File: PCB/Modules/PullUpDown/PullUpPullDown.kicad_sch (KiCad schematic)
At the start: 7 parts

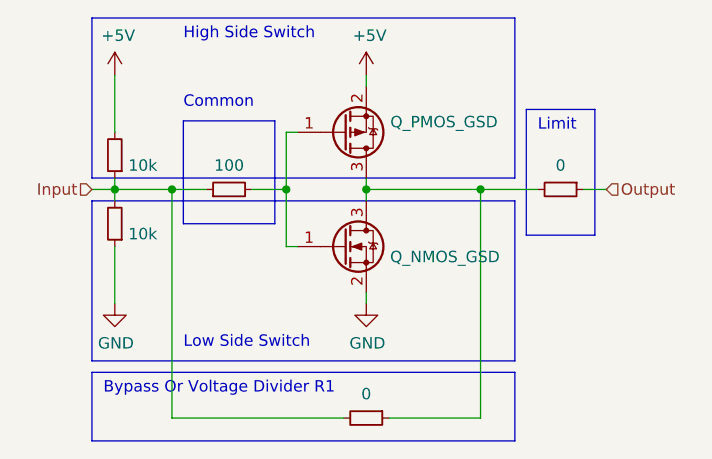
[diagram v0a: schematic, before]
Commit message: Upgrade KiCad files from 6.0 to 7.0.
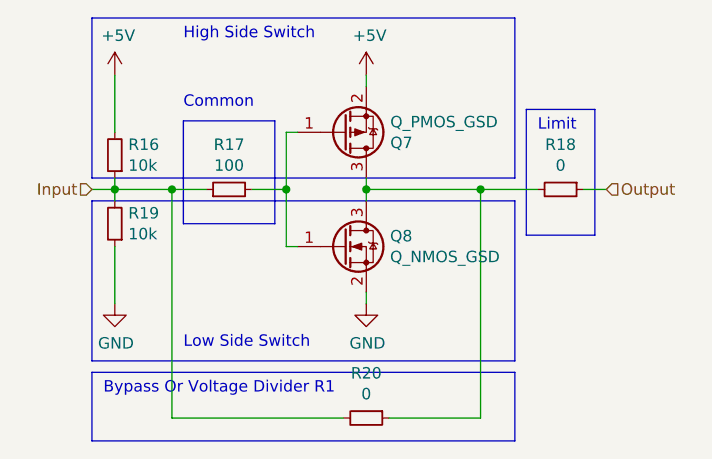
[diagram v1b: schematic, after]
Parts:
- gave numbers to parts that had none: 7

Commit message: First pass of PCB rework.
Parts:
- removed R20: 0, Resistor_SMD:R_0805_2012Metric, symbol Device:R_Small
- added JP1: Bypass, Jumper:SolderJumper-2_P1.3mm_Open_RoundedPad1.0x1.5mm, symbol Jumper:SolderJumper_2_Open
- renumbered Q7 to Q1, Q8 to Q2, R16 to R1, R19 to R2, R17 to R3, R18 to R4
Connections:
- net Input: now also JP1.1 (A)
- net at Q1.3 (D), Q2.3 (D), R4.2: now also JP1.2 (B)
- net +5V renamed +3.3V
- net +3.3V: no longer Q1.2 (S)
- new net VCC: Q1.2 (S)
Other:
- note added: "Bypass Jumper"
- note added: "Limit / Voltage Divider R1"
- note removed: "Bypass Or Voltage Divider R1"
- note removed: "Limit"
- moved on the sheet: Q1, Q2, R1, R2, R3, R4

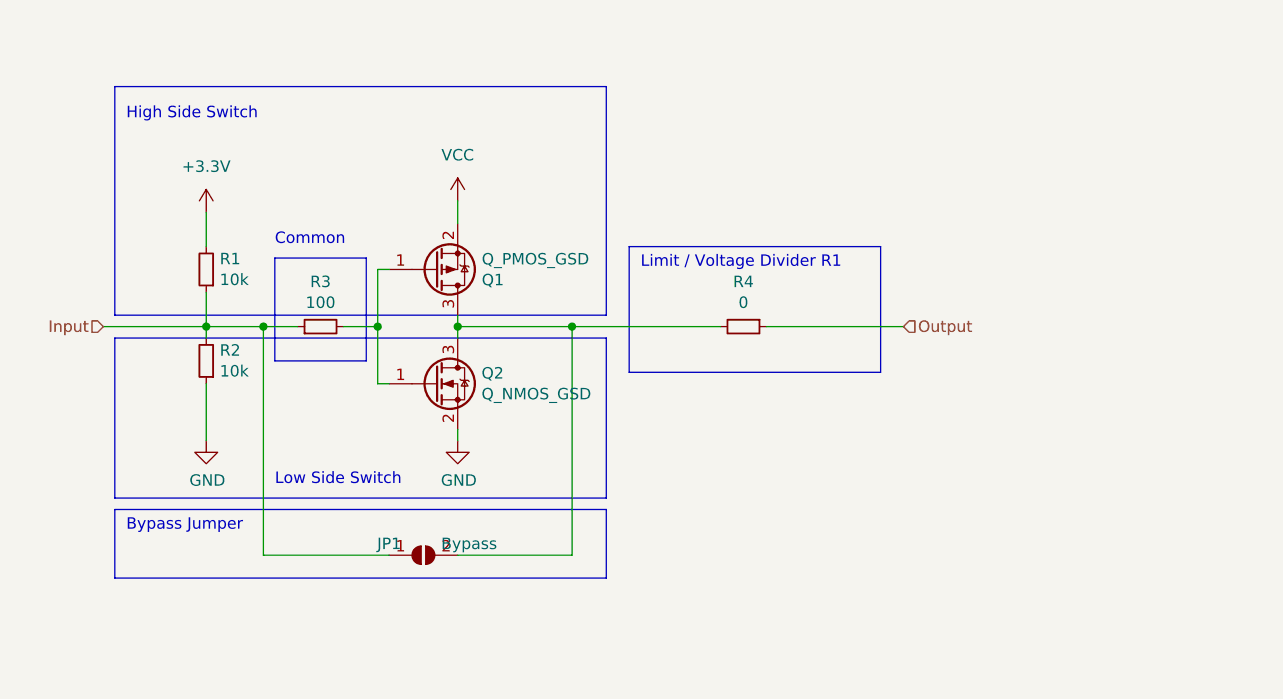
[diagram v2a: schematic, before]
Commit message: Update pull up/down module, with multivoltage ESD protection.
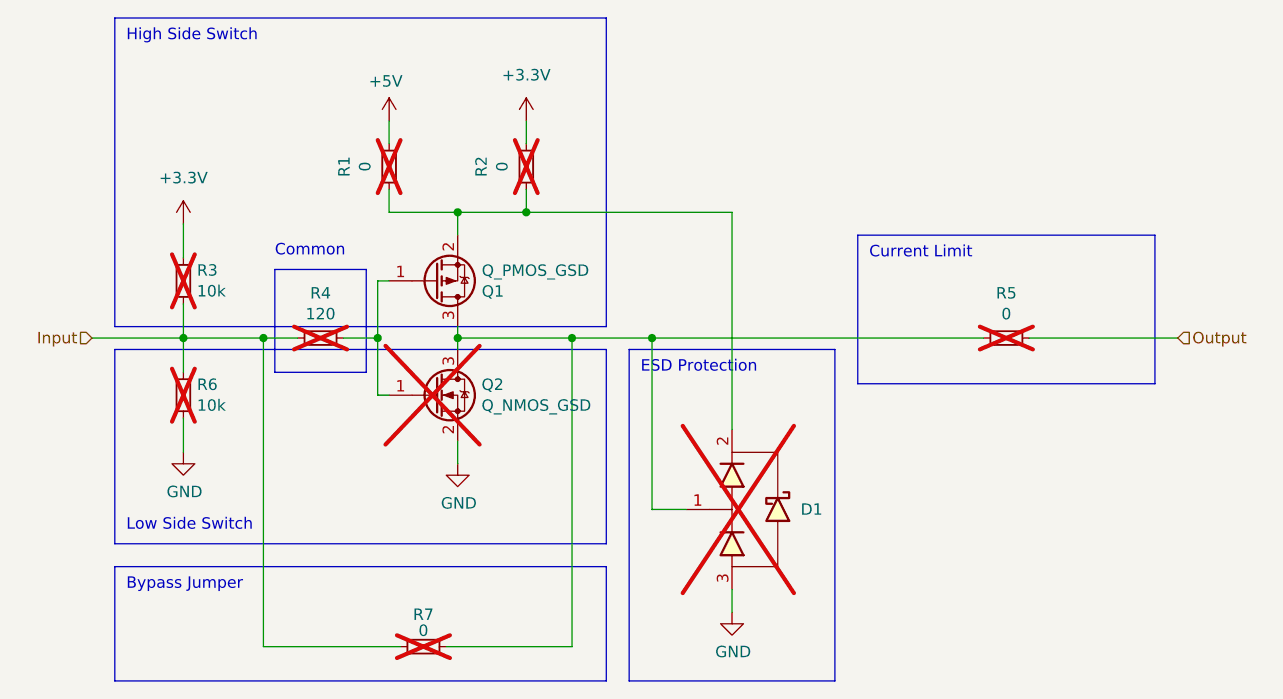
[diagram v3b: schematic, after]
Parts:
- removed JP1: Bypass, Jumper:SolderJumper-2_P1.3mm_Open_RoundedPad1.0x1.5mm, symbol Jumper:SolderJumper_2_Open
- added D1: D1213A-01SO-7, Package_TO_SOT_SMD:SOT-23, symbol KTANE:D1213A-01SO-7
- added R1, R2, R7: 0, Resistor_SMD:R_0603_1608Metric, symbol Device:R_Small
- Q1: DIGIKEY (none) -> DMG2301L-7DICT-ND
- Q2: DIGIKEY (none) -> 31-DMN2310U-7CT-ND; now not fitted
- R3: renamed from R1; footprint Resistor_SMD:R_0805_2012Metric -> Resistor_SMD:R_0603_1608Metric; DIGIKEY (none) -> P10.0KHCT-ND; now not fitted
- R4: renamed from R3; value 100 -> 120; footprint Resistor_SMD:R_0805_2012Metric -> Resistor_SMD:R_0603_1608Metric; DIGIKEY (none) -> P120HCT-ND; now not fitted
- R5: renamed from R4; footprint Resistor_SMD:R_0805_2012Metric -> Resistor_SMD:R_0603_1608Metric; DIGIKEY (none) -> 10-ERJ-H3G0R00VCT-ND; now not fitted
- R6: renamed from R2; footprint Resistor_SMD:R_0805_2012Metric -> Resistor_SMD:R_0603_1608Metric; DIGIKEY (none) -> P10.0KHCT-ND; now not fitted
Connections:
- net +3.3V: now also R2.1
- net GND: now also D1.3
- net Input: now also R7.2
- net at Q1.3 (D), Q2.3 (D), R5.2: now also D1.1, R7.1
- net VCC: no longer names the net of Q1.2 (S)
- net VCC: now also D1.2, R1.2, R2.2
- new net +5V: R1.1
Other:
- note added: "Current Limit"
- note added: "ESD Protection"
- note removed: "Limit / Voltage Divider R1"
- moved on the sheet: Q1
